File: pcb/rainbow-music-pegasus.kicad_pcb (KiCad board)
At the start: 2 copper layers, 150.7 x 30.5 mm, 107 parts, among them J1 USB_B_Micro, J2 Conn_02x03_Odd_Even, J3 B2B-PH-K-S, Q1 DMG3415U, SW1 SW_SPDT, SW2 EVQQ2, U1 ESP32-C3-MINI-1, U2 OPA344NA, U3 TLV75533PDBV, U4 MCP73831-2-OT

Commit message: Increase the size of Altivo's picture on the back silkscreen
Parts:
- moved G*** 1.69 mm to (98.1, 93.8)

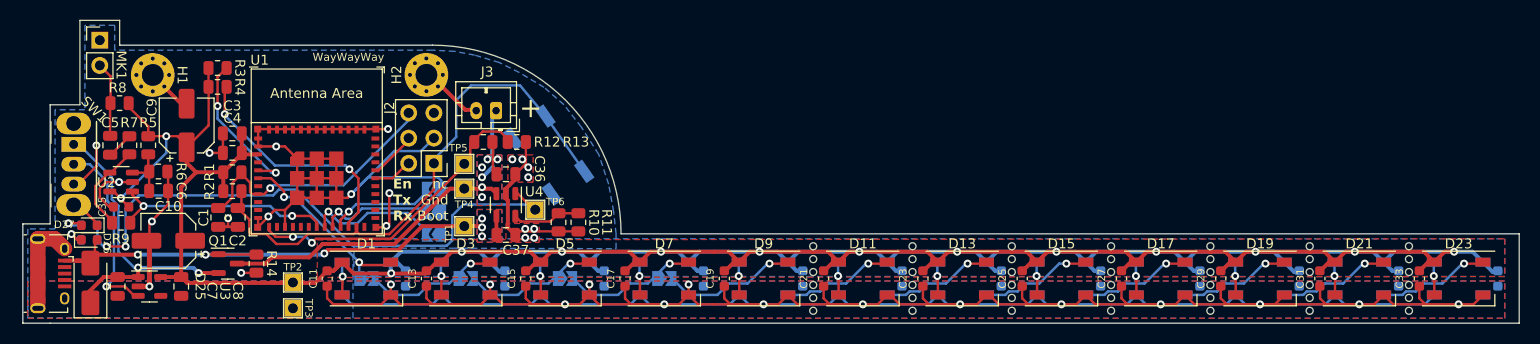
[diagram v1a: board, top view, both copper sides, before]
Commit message: Updated schematics.pdf to v1.1 design, link to KiCanvas
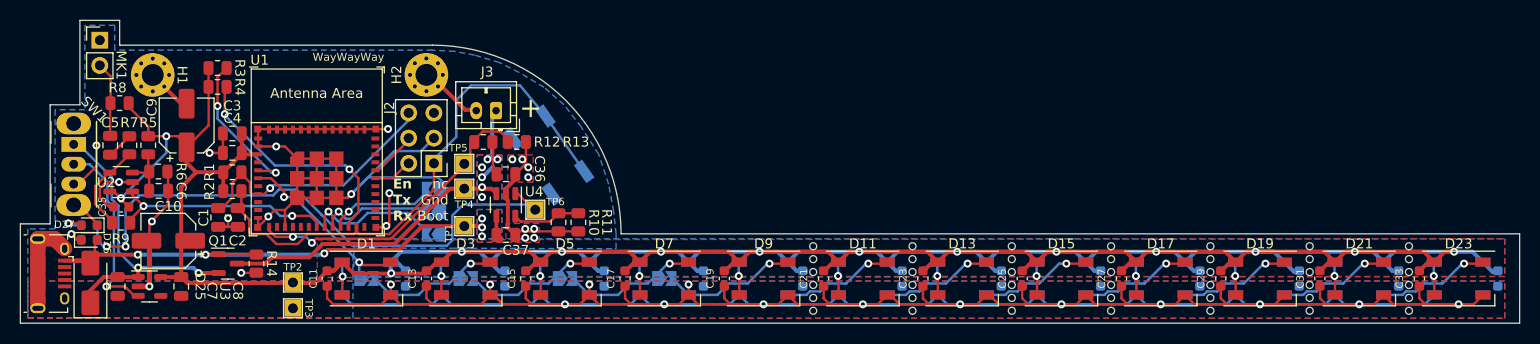
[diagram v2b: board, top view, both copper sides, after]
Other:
- board size 150.7 x 30.5 mm -> 151 x 30.5 mm
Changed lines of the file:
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@@
     )
     (pad_to_mask_clearance 0)
-    (grid_origin 231.908384 96.1)
+    (grid_origin 80.9475 105.1)
     (pcbplotparams
       (layerselection 0x00010fc_ffffffff)
@@
       ))
   )
-  (gr_line (start 231.908384 105.1) (end 83.9475 105.1)
+  (gr_line (start 231.9475 105.1) (end 80.9475 105.1)
     (stroke (width 0.1) (type default)) (layer "Edge.Cuts"))
   (gr_circle (center 170.8 103.85) (end 171.05 104.1)
@@
   (gr_line (start 90.9475 74.6) (end 90.9475 74.6)
     (stroke (width 0.1) (type default)) (layer "Edge.Cuts"))
-  (gr_line (start 81.1975 95.1) (end 81.1975 105.1)
+  (gr_line (start 80.9475 95.1) (end 80.9475 105.1)
     (stroke (width 0.1) (type default)) (layer "Edge.Cuts"))
   (gr_circle (center 180.8 101.25) (end 181.05 101.5)
@@
   (gr_circle (center 210.8 97.35) (end 211.05 97.6)
     (stroke (width 0.1) (type default)) (fill none) (layer "Edge.Cuts"))
-  (gr_line (start 83.9475 95.1) (end 81.1975 95.1)
+  (gr_line (start 83.9475 95.1) (end 80.9475 95.1)
     (stroke (width 0.1) (type default)) (layer "Edge.Cuts"))
   (gr_circle (center 170.8 97.35) (end 171.05 97.6)
@@
   (gr_circle (center 180.8 97.35) (end 181.05 97.6)
     (stroke (width 0.1) (type default)) (fill none) (layer "Edge.Cuts"))
-  (gr_line (start 231.908384 96.1) (end 231.908384 105.1)
+  (gr_line (start 231.9475 96.1) (end 231.9475 105.1)
     (stroke (width 0.1) (type default)) (layer "Edge.Cuts"))
   (gr_circle (center 170.8 101.25) (end 171.05 101.5)
@@
   (gr_circle (center 170.8 99.95) (end 171.05 100.2)
     (stroke (width 0.1) (type default)) (fill none) (layer "Edge.Cuts"))
-  (gr_line (start 81.1975 105.1) (end 83.9475 105.1)
-    (stroke (width 0.1) (type default)) (layer "Edge.Cuts"))
   (gr_circle (center 200.8 99.95) (end 201.05 100.2)
     (stroke (width 0.1) (type default)) (fill none) (layer "Edge.Cuts"))
@@
   (gr_circle (center 210.8 98.65) (end 211.05 98.9)
     (stroke (width 0.1) (type default)) (fill none) (layer "Edge.Cuts"))
-  (gr_line (start 141.4475 96.1) (end 231.908384 96.1)
+  (gr_line (start 141.4475 96.1) (end 231.9475 96.1)
     (stroke (width 0.1) (type default)) (layer "Edge.Cuts"))
   (gr_text "v1.1" (at 109.568384 98.96) (layer "B.SilkS")
@@
   )
   (dimension (type aligned) (layer "Cmts.User")
-    (pts (xy 83.9475 105.1) (xy 83.9475 74.6))
-    (height -2)
-    (gr_text "30.5 mm" (at 80.7975 89.85 90) (layer "Cmts.User")
+    (pts (xy 83.9475 95.1) (xy 83.9475 83.1))
+    (height -5.229116)
+    (gr_text "12 mm" (at 77.568384 89.1 90) (layer "Cmts.User")
+      (effects (font (size 1 1) (thickness 0.15)))
+    )
+    (format (prefix "") (suffix "") (units 3) (units_format 1) (precision 4) suppress_zeroes)
+    (style (thickness 0.15) (arrow_length 1.27) (text_position_mode 0) (extension_height 0.58642) (extension_offset 0.5) keep_text_aligned)
+  )
+  (dimension (type aligned) (layer "Cmts.User")
+    (pts (xy 122.4475 77.1) (xy 141.4475 77.1))
+    (height -4)
+    (gr_text "19 mm" (at 131.9475 71.95) (layer "Cmts.User")
       (effects (font (size 1 1) (thickness 0.15)))
     )
@@
   )
   (dimension (type aligned) (layer "Cmts.User")
-    (pts (xy 143.9475 96.1) (xy 221.9475 96.1))
-    (height -2.2)
-    (gr_text "78 mm" (at 182.9475 92.75) (layer "Cmts.User")
+    (pts (xy 141.4475 96.1) (xy 231.9475 96.1))
+    (height -2.19)
+    (gr_text "90.5 mm" (at 186.6975 92.76) (layer "Cmts.User")
       (effects (font (size 1 1) (thickness 0.15)))
     )
@@
   )
   (dimension (type aligned) (layer "Cmts.User")
-    (pts (xy 221.9475 96.1) (xy 221.9475 105.1))
+    (pts (xy 231.908384 96.1) (xy 231.908384 105.1))
     (height -2.5)
-    (gr_text "9 mm" (at 223.2975 100.6 90) (layer "Cmts.User")
+    (gr_text "9 mm" (at 233.258384 100.6 90) (layer "Cmts.User")
       (effects (font (size 1 1) (thickness 0.15)))
     )
@@
   )
   (dimension (type aligned) (layer "Cmts.User")
-    (pts (xy 221.9475 105.1) (xy 83.9475 105.1))
+    (pts (xy 90.9475 74.6) (xy 90.9475 77.1))
     (height -2.5)
-    (gr_text "138 mm" (at 152.9475 106.45) (layer "Cmts.User")
+    (gr_text "2.5 mm" (at 97.4475 75.85) (layer "Cmts.User")
+      (effects (font (size 1 1) (thickness 0.15)))
+    )
+    (format (prefix "") (suffix "") (units 3) (units_format 1) (precision 4) suppress_zeroes)
+    (style (thickness 0.15) (arrow_length 1.27) (text_position_mode 2) (extension_height 0.58642) (extension_offset 0.5))
+  )
+  (dimension (type aligned) (layer "Cmts.User")
+    (pts (xy 231.9475 105.1) (xy 80.9475 105.1))
+    (height -2.5)
+    (gr_text "151 mm" (at 156.4475 106.45) (layer "Cmts.User")
       (effects (font (size 1 1) (thickness 0.15)))
     )
@@
   )
   (dimension (type aligned) (layer "Cmts.User")
-    (pts (xy 143.5475 77.1) (xy 143.5475 96.1))
+    (pts (xy 83.9475 95.1) (xy 80.9475 95.1))
+    (height 22)
+    (gr_text "3 mm" (at 82.4475 70.1 90) (layer "Cmts.User")
+      (effects (font (size 1 1) (thickness 0.15)))
+    )
+    (format (prefix "") (suffix "") (units 3) (units_format 1) (precision 4) suppress_zeroes)
+    (style (thickness 0.15) (arrow_length 1.27) (text_position_mode 2) (extension_height 0.58642) (extension_offset 0.5))
+  )
+  (dimension (type aligned) (layer "Cmts.User")
+    (pts (xy 141.4475 77.1) (xy 141.4475 96.1))
     (height -2.4)
-    (gr_text "19 mm" (at 144.7975 86.6 90) (layer "Cmts.User")
+    (gr_text "19 mm" (at 142.6975 86.6 90) (layer "Cmts.User")
       (effects (font (size 1 1) (thickness 0.15)))
     )
@@
   )
   (dimension (type aligned) (layer "Cmts.User")
-    (pts (xy 90.9475 77.1) (xy 124.9475 77.1))
+    (pts (xy 90.9475 77.1) (xy 122.4475 77.1))
     (height -4)
-    (gr_text "34 mm" (at 107.9475 71.95) (layer "Cmts.User")
+    (gr_text "31.5 mm" (at 106.6975 71.95) (layer "Cmts.User")
+      (effects (font (size 1 1) (thickness 0.15)))
+    )
+    (format (prefix "") (suffix "") (units 3) (units_format 1) (precision 4) suppress_zeroes)
+    (style (thickness 0.15) (arrow_length 1.27) (text_position_mode 0) (extension_height 0.58642) (extension_offset 0.5) keep_text_aligned)
+  )
+  (dimension (type aligned) (layer "Cmts.User")
+    (pts (xy 81.1975 105.1) (xy 81.1975 95.1))
+    (height -2.479116)
+    (gr_text "10 mm" (at 77.568384 100.1 90) (layer "Cmts.User")
       (effects (font (size 1 1) (thickness 0.15)))
     )
@@
   (dimension (type aligned) (layer "Cmts.User")
     (pts (xy 83.9475 83.1) (xy 86.9475 83.1))
-    (height -12.5)
-    (gr_text "3 mm" (at 85.4475 69.45) (layer "Cmts.User")
+    (height -10)
+    (gr_text "3 mm" (at 85.4475 70.1 90) (layer "Cmts.User")
+      (effects (font (size 1 1) (thickness 0.15)))
+    )
+    (format (prefix "") (suffix "") (units 3) (units_format 1) (precision 4) suppress_zeroes)
+    (style (thickness 0.15) (arrow_length 1.27) (text_position_mode 2) (extension_height 0.58642) (extension_offset 0.5))
+  )
+  (dimension (type orthogonal) (layer "Cmts.User")
+    (pts (xy 86.9475 74.6) (xy 80.9475 105.1))
+    (height -11)
+    (orientation 1)
+    (gr_text "30.5 mm" (at 74.7975 89.85 90) (layer "Cmts.User")
+      (effects (font (size 1 1) (thickness 0.15)))
+    )
+    (format (prefix "") (suffix "") (units 3) (units_format 1) (precision 4) suppress_zeroes)
+    (style (thickness 0.15) (arrow_length 1.27) (text_position_mode 0) (extension_height 0.58642) (extension_offset 0.5) keep_text_aligned)
+  )
+  (dimension (type orthogonal) (layer "Cmts.User")
+    (pts (xy 80.9475 95.1) (xy 141.4475 96.1))
+    (height -28)
+    (orientation 0)
+    (gr_text "60.5 mm" (at 111.1975 65.95) (layer "Cmts.User")
       (effects (font (size 1 1) (thickness 0.15)))
     )

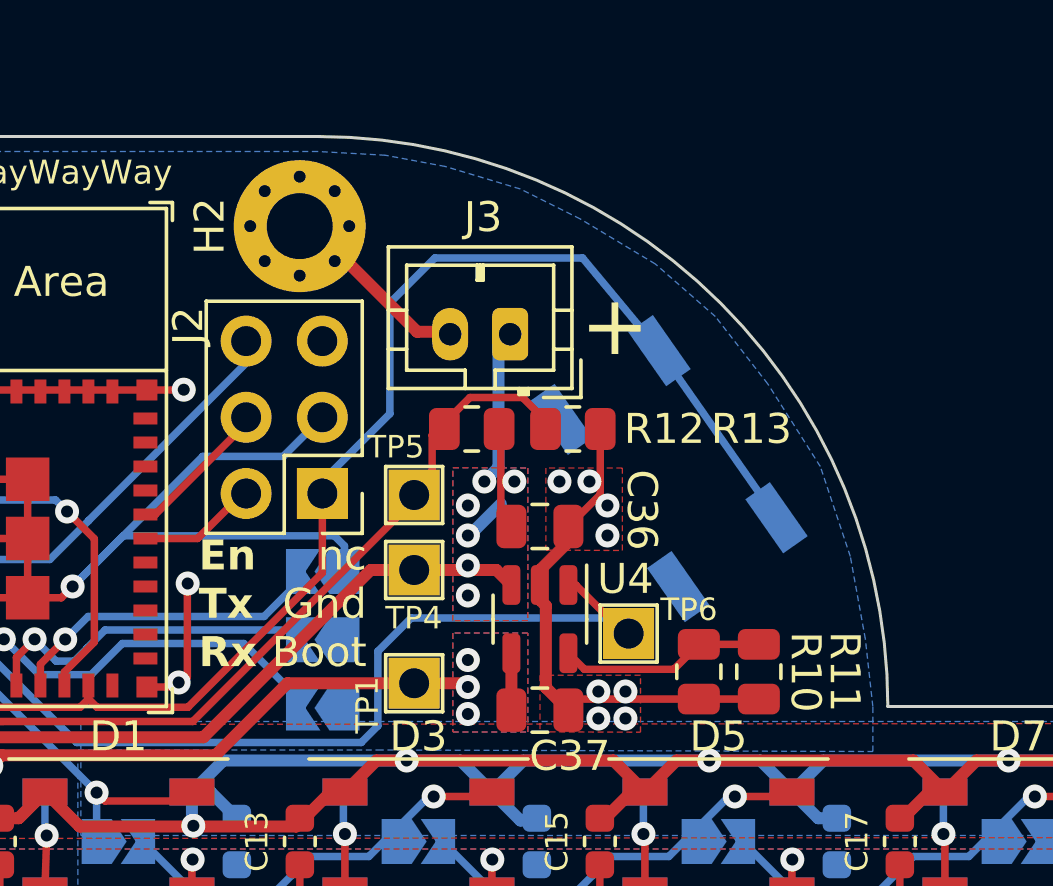
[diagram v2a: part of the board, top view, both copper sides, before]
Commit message: Round out the ground fill zone using an arc margin
Looks much nicer than eyeballing the fill zone into an arc-like shape by
point
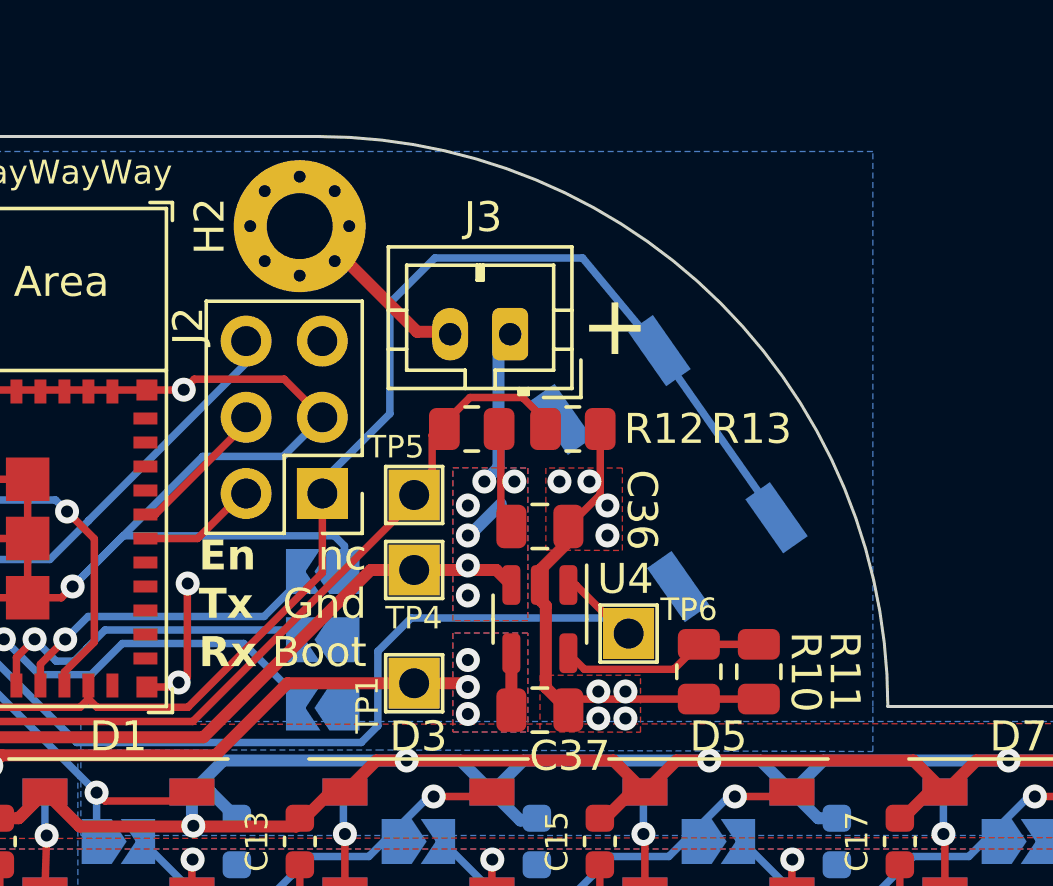
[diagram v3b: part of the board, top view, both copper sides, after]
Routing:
- net GND: track 462.3 -> 467.6 mm
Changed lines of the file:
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@@
     )
     (pad_to_mask_clearance 0)
-    (grid_origin 80.9475 105.1)
+    (grid_origin 122.4475 77.1)
     (pcbplotparams
       (layerselection 0x00010fc_ffffffff)
@@
   (gr_line (start 141.4475 96.1) (end 231.9475 96.1)
     (stroke (width 0.1) (type default)) (layer "Edge.Cuts"))
+  (gr_arc (start 122.447561 77.5025) (mid 135.57419 82.959441) (end 140.9975 96.1)
+    (stroke (width 0.1) (type default)) (layer "Margin"))
   (gr_text "v1.1" (at 109.568384 98.96) (layer "B.SilkS")
     (effects (font (size 1 1) (thickness 0.15)) (justify bottom mirror))
@@
   )
   (dimension (type orthogonal) (layer "Cmts.User")
+    (pts (xy 80.9475 105.1) (xy 115.8 100.6))
+    (height 5.15)
+    (orientation 0)
+    (gr_text "34.8525 mm" (at 98.37375 109.1) (layer "Cmts.User")
+      (effects (font (size 1 1) (thickness 0.15)))
+    )
+    (format (prefix "") (suffix "") (units 3) (units_format 1) (precision 4))
+    (style (thickness 0.15) (arrow_length 1.27) (text_position_mode 0) (extension_height 0.58642) (extension_offset 0.5) keep_text_aligned)
+  )
+  (dimension (type orthogonal) (layer "Cmts.User")
     (pts (xy 86.9475 74.6) (xy 80.9475 105.1))
     (height -11)
@@
   (segment (start 118.0975 95.119152) (end 117.916652 95.3) (width 0.25) (layer "F.Cu") (net 1))
   (segment (start 141.8475 102.5975) (end 142.45 103.2) (width 0.25) (layer "F.Cu") (net 1))
+  (segment (start 121.3275 85.19) (end 122.5975 86.46) (width 0.25) (layer "F.Cu") (net 1))
   (segment (start 189.2 103.2) (end 195.8 103.2) (width 0.25) (layer "F.Cu") (net 1))
   (segment (start 93.394251 101.4) (end 93.394251 101.4) (width 0.5) (layer "F.Cu") (net 1))
@@
   (segment (start 211.8475 101.375) (end 211.8475 102.5975) (width 0.25) (layer "F.Cu") (net 1))
   (segment (start 131.165 95.8525) (end 130.7975 96.22) (width 0.25) (layer "F.Cu") (net 1))
+  (segment (start 118.3275 85.19) (end 121.3275 85.19) (width 0.25) (layer "F.Cu") (net 1))
   (segment (start 116.75 85.55) (end 117.9675 85.55) (width 0.25) (layer "F.Cu") (net 1))
   (segment (start 129.55 103.2) (end 135.8 103.2) (width 0.25) (layer "F.Cu") (net 1))
@@
   (segment (start 118.25 101.212797) (end 118.25 102.25) (width 0.25) (layer "F.Cu") (net 1))
   (segment (start 97.1375 82.99) (end 94.280774 80.133274) (width 0.4) (layer "F.Cu") (net 1))
+  (segment (start 117.9775 85.54) (end 118.3275 85.19) (width 0.25) (layer "F.Cu") (net 1))
   (segment (start 105.923 94.35) (end 105.923 94.377) (width 0.25) (layer "F.Cu") (net 1))
   (segment (start 199.2 103.2) (end 198.25 102.25) (width 0.25) (layer "F.Cu") (net 1))
@@
       (pts
         (xy 140.9475 96.1)
-        (xy 140.6975 93.85)
-        (xy 140.1975 91.1)
-        (xy 139.1975 88.101237)
-        (xy 137.4475 85.35)
-        (xy 135.6975 83.1)
-        (xy 133.6975 81.35)
-        (xy 131.1975 79.85)
-        (xy 129.1975 78.85)
-        (xy 126.6975 78.1)
-        (xy 124.6975 77.725)
+        (xy 140.9475 77.6)
         (xy 122.4475 77.6)
         (xy 90.4475 77.6)
